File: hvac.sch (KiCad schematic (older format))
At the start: 44 parts, among them CN1 1X4-3.5MM, IC1 ATMEGA328P-A, J1 PROGRAMMING HEADER, J2 SERIAL PORT, J3 POWER_INPUT, J4 1X2-3.5MM, SW1 SPST, SW2 SPST, SW3 SPST, U1 MIC5225, U2 MOSFET_N, U3 MOSFET_N, U4 MOSFET_N

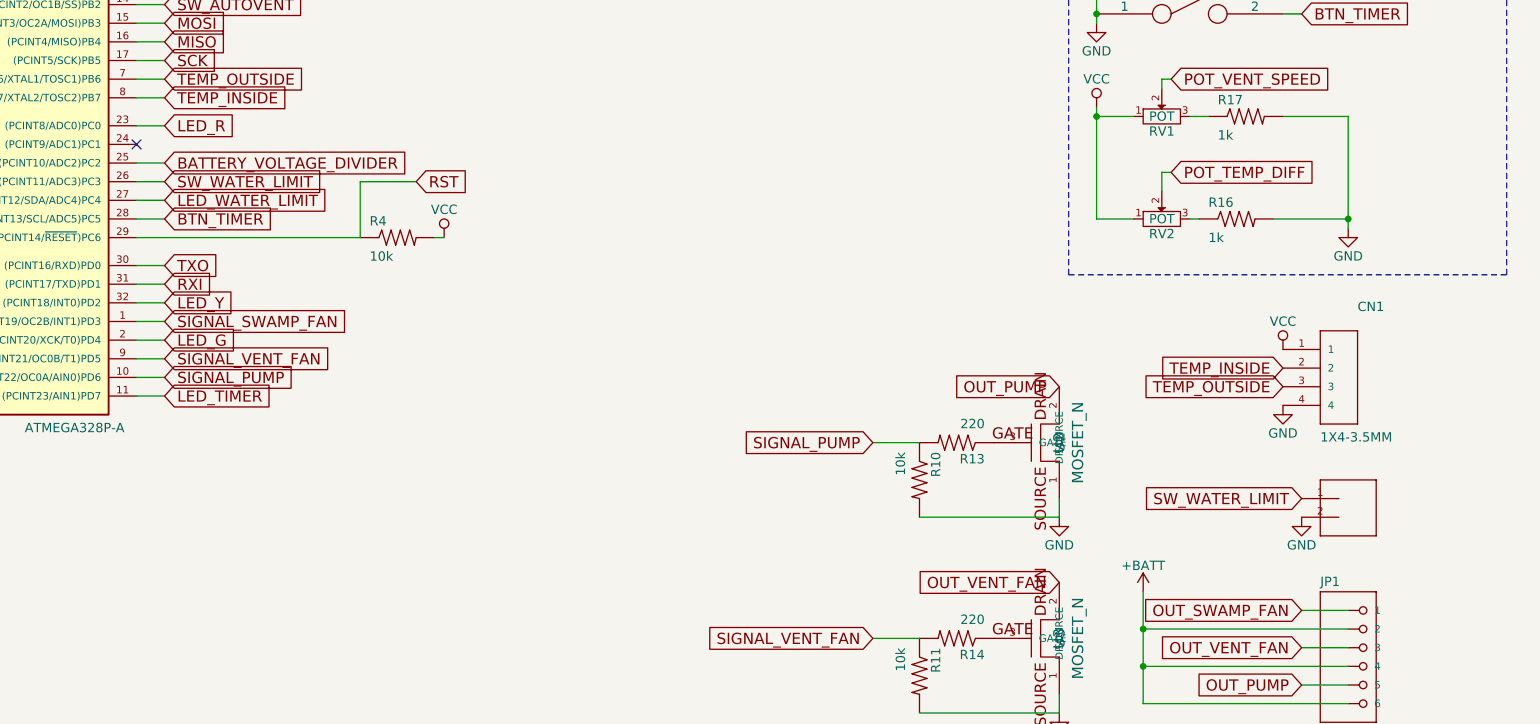
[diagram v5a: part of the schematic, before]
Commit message: Switch to 6 pin header
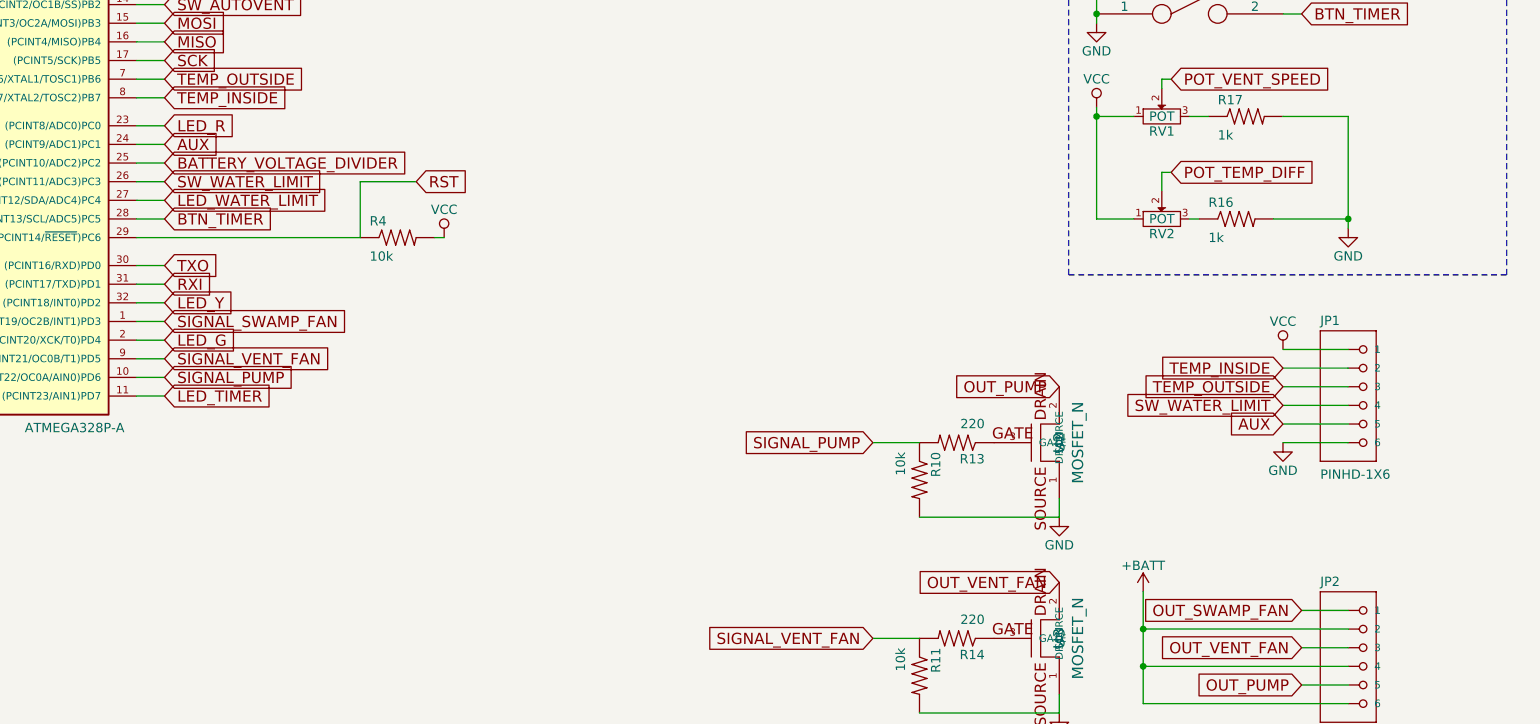
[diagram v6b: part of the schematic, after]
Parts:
- removed CN1: 1X4-3.5MM, 1X04-3.5MM, symbol 1X4-3.5MM
- removed J4: 1X2-3.5MM, 1X2-3.5MM, symbol 1X2-3.5MM
- added JP1: PINHD-1X6, 1X06, symbol PINHD-1X6
- renumbered JP1 to JP2
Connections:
- net GND: now also JP1.6
- net SW_WATER_LIMIT: now also JP1.4
- net TEMP_INSIDE: now also JP1.2
- net TEMP_OUTSIDE: now also JP1.3
- net VCC: now also JP1.1
- net AUX: now reaches IC1.24 ((PCINT9/ADC1)PC1)
- net AUX: now also JP1.5
- no-connect marks 1 -> 0
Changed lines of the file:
@@
 Wire Wire Line
 	750  7300 900  7300
-NoConn ~ 3850 2150
 Text GLabel 4000 2900 2    60   Input ~ 0
 RXI
@@
 Text Notes 10550 600  0    60   ~ 0
 Human inputs
-$Comp
-L 1X4-3.5MM CN1
-U 1 1 590F71DF
-P 10200 3350
-F 0 "CN1" H 10400 3650 50  0000 L BNN
-F 1 "1X4-3.5MM" H 10200 2950 50  0000 L BNN
-F 2 "1X04-3.5MM" H 10230 3500 20  0001 C CNN
-F 3 "" H 10200 3350 60  0000 C CNN
-	1    10200 3350
-	1    0    0    -1
-$EndComp
 Text GLabel 10000 3350 0    60   Input ~ 0
 TEMP_INSIDE
@@
 $Comp
 L GND #PWR023
-U 1 1 590F7CE7
-P 10000 3550
-F 0 "#PWR023" H 10000 3300 50  0001 C CNN
-F 1 "GND" H 10000 3400 50  0000 C CNN
-F 2 "" H 10000 3550 50  0000 C CNN
-F 3 "" H 10000 3550 50  0000 C CNN
-	1    10000 3550
-	1    0    0    -1
-$EndComp
-$Comp
-L GND #PWR024
 U 1 1 590FA0A9
 P 4600 6150
-F 0 "#PWR024" H 4600 5900 50  0001 C CNN
+F 0 "#PWR023" H 4600 5900 50  0001 C CNN
 F 1 "GND" H 4600 6000 50  0000 C CNN
 F 2 "" H 4600 6150 50  0000 C CNN
@@
 $EndComp
 $Comp
-L +BATT #PWR025
+L +BATT #PWR024
 U 1 1 590FA14E
 P 3800 6050
-F 0 "#PWR025" H 3800 5900 50  0001 C CNN
+F 0 "#PWR024" H 3800 5900 50  0001 C CNN
 F 1 "+BATT" H 3800 6190 50  0000 C CNN
 F 2 "" H 3800 6050 50  0000 C CNN
@@
 Power Connector
 $Comp
-L GND #PWR026
+L GND #PWR025
 U 1 1 590FBCD1
 P 3100 7550
-F 0 "#PWR026" H 3100 7300 50  0001 C CNN
+F 0 "#PWR025" H 3100 7300 50  0001 C CNN
 F 1 "GND" H 3100 7400 50  0000 C CNN
 F 2 "" H 3100 7550 50  0000 C CNN
@@
 $EndComp
 $Comp
-L +BATT #PWR027
+L +BATT #PWR026
 U 1 1 590FC073
 P 3100 6450
-F 0 "#PWR027" H 3100 6300 50  0001 C CNN
+F 0 "#PWR026" H 3100 6300 50  0001 C CNN
 F 1 "+BATT" H 3100 6590 50  0000 C CNN
 F 2 "" H 3100 6450 50  0000 C CNN
@@
 Programming Ports
 $Comp
-L 1X2-3.5MM J4
-U 1 1 590FE1C1
-P 10300 4150
-F 0 "J4" H 10300 4150 50  0001 C CNN
-F 1 "1X2-3.5MM" H 10300 4150 50  0001 C CNN
-F 2 "1X2-3.5MM" H 10330 4300 20  0001 C CNN
-F 3 "" H 10300 4150 60  0000 C CNN
-	1    10300 4150
-	1    0    0    -1
-$EndComp
-$Comp
-L GND #PWR028
+L GND #PWR027
 U 1 1 590FE215
-P 10100 4150
-F 0 "#PWR028" H 10100 3900 50  0001 C CNN
-F 1 "GND" H 10100 4000 50  0000 C CNN
-F 2 "" H 10100 4150 50  0000 C CNN
-F 3 "" H 10100 4150 50  0000 C CNN
-	1    10100 4150
-	1    0    0    -1
-$EndComp
-Text GLabel 10100 4050 0    60   Input ~ 0
+P 10000 3750
+F 0 "#PWR027" H 10000 3500 50  0001 C CNN
+F 1 "GND" H 10000 3600 50  0000 C CNN
+F 2 "" H 10000 3750 50  0000 C CNN
+F 3 "" H 10000 3750 50  0000 C CNN
+	1    10000 3750
+	1    0    0    -1
+$EndComp
+Text GLabel 10000 3550 0    60   Input ~ 0
 SW_WATER_LIMIT
 Text GLabel 7800 4800 0    60   Input ~ 0
@@
 OUT_PUMP
 $Comp
-L PINHD-1X6 JP1
+L PINHD-1X6 JP2
 U 1 1 590FEE3F
 P 10450 4950
-F 0 "JP1" H 10200 5375 50  0000 L BNN
+F 0 "JP2" H 10200 5375 50  0000 L BNN
 F 1 "PINHD-1X6" H 10200 4550 50  0000 L BNN
 F 2 "1X06" H 10480 5100 20  0001 C CNN
@@
 $EndComp
 $Comp
-L GND #PWR029
+L GND #PWR028
 U 1 1 59102A56
 P 8800 5200
-F 0 "#PWR029" H 8800 4950 50  0001 C CNN
+F 0 "#PWR028" H 8800 4950 50  0001 C CNN
 F 1 "GND" H 8800 5050 50  0000 C CNN
 F 2 "" H 8800 5200 50  0000 C CNN
@@
 $EndComp
 $Comp
-L +BATT #PWR030
+L +BATT #PWR029
 U 1 1 59102C3A
 P 9250 4550
-F 0 "#PWR030" H 9250 4400 50  0001 C CNN
+F 0 "#PWR029" H 9250 4400 50  0001 C CNN
 F 1 "+BATT" H 9250 4690 50  0000 C CNN
 F 2 "" H 9250 4550 50  0000 C CNN
@@
 $EndComp
 $Comp
-L GND #PWR031
+L GND #PWR030
 U 1 1 591065E6
 P 8800 6250
-F 0 "#PWR031" H 8800 6000 50  0001 C CNN
+F 0 "#PWR030" H 8800 6000 50  0001 C CNN
 F 1 "GND" H 8800 6100 50  0000 C CNN
 F 2 "" H 8800 6250 50  0000 C CNN
@@
 $EndComp
 $Comp
-L GND #PWR032
+L GND #PWR031
 U 1 1 591067B3
 P 8800 4150
-F 0 "#PWR032" H 8800 3900 50  0001 C CNN
+F 0 "#PWR031" H 8800 3900 50  0001 C CNN
 F 1 "GND" H 8800 4000 50  0000 C CNN
 F 2 "" H 8800 4150 50  0000 C CNN
@@
 Wire Wire Line
 	8800 5200 8050 5200
+$Comp
+L PINHD-1X6 JP1
+U 1 1 5910D38E
+P 10450 3550
+F 0 "JP1" H 10200 3975 50  0000 L BNN
+F 1 "PINHD-1X6" H 10200 3150 50  0000 L BNN
+F 2 "1X06" H 10480 3700 20  0001 C CNN
+F 3 "" H 10450 3550 60  0000 C CNN
+	1    10450 3550
+	1    0    0    -1
+$EndComp
+Text GLabel 4000 2150 2    60   Input ~ 0
+AUX
+Wire Wire Line
+	4000 2150 3850 2150
+Wire Wire Line
+	10000 3750 10350 3750
+Wire Wire Line
+	10350 3650 10000 3650
+Text GLabel 10000 3650 0    60   Input ~ 0
+AUX
+Wire Wire Line
+	10000 3550 10350 3550
+Wire Wire Line
+	10350 3450 10000 3450
+Wire Wire Line
+	10000 3350 10350 3350
+Wire Wire Line
+	10350 3250 10000 3250
 $EndSCHEMATC
